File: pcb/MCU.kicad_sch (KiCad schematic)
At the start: 10 parts, among them U1 WeMos_S2_mini

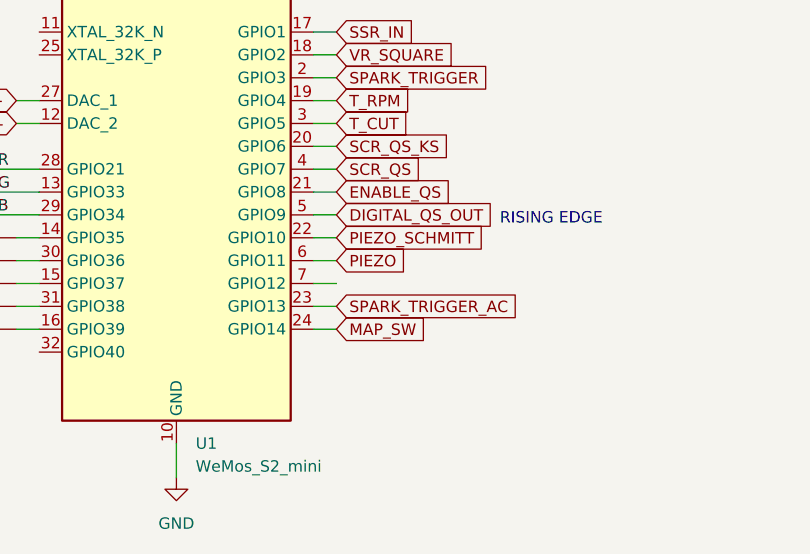
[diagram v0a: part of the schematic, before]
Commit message: widely changed TCI schematic to use a FET IC driver
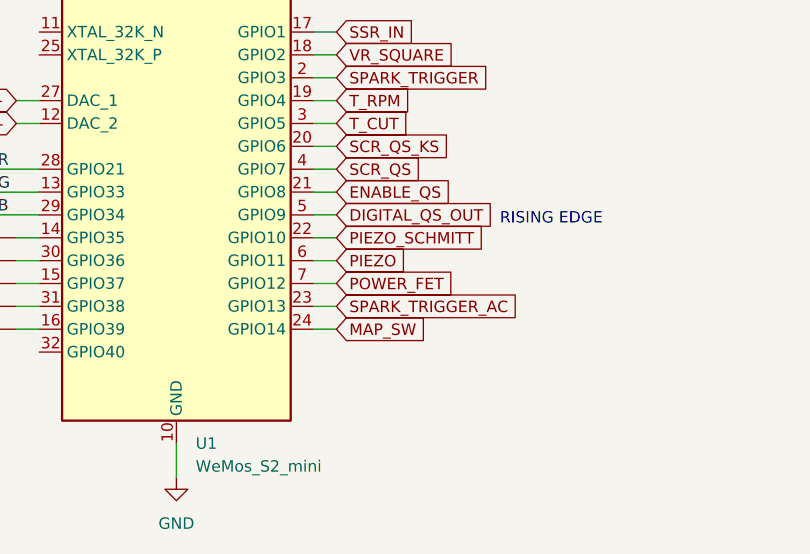
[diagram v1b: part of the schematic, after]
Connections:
- net POWER_FET: now reaches U1.7 (GPIO12)
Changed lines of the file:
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@@
+		)
+	)
+	(global_label "POWER_FET"
+		(shape input)
+		(at 106.68 80.01 0)
+		(fields_autoplaced yes)
+		(effects
+			(font
+				(size 1.27 1.27)
+			)
+			(justify left)
+		)
+		(property "Intersheetrefs" "${INTERSHEET_REFS}"
+			(at 120.3089 80.01 0)
+			(effects
+				(font
+					(size 1.27 1.27)
+				)
+				(justify left)
+				(hide yes)
+			)
 		)
 	)

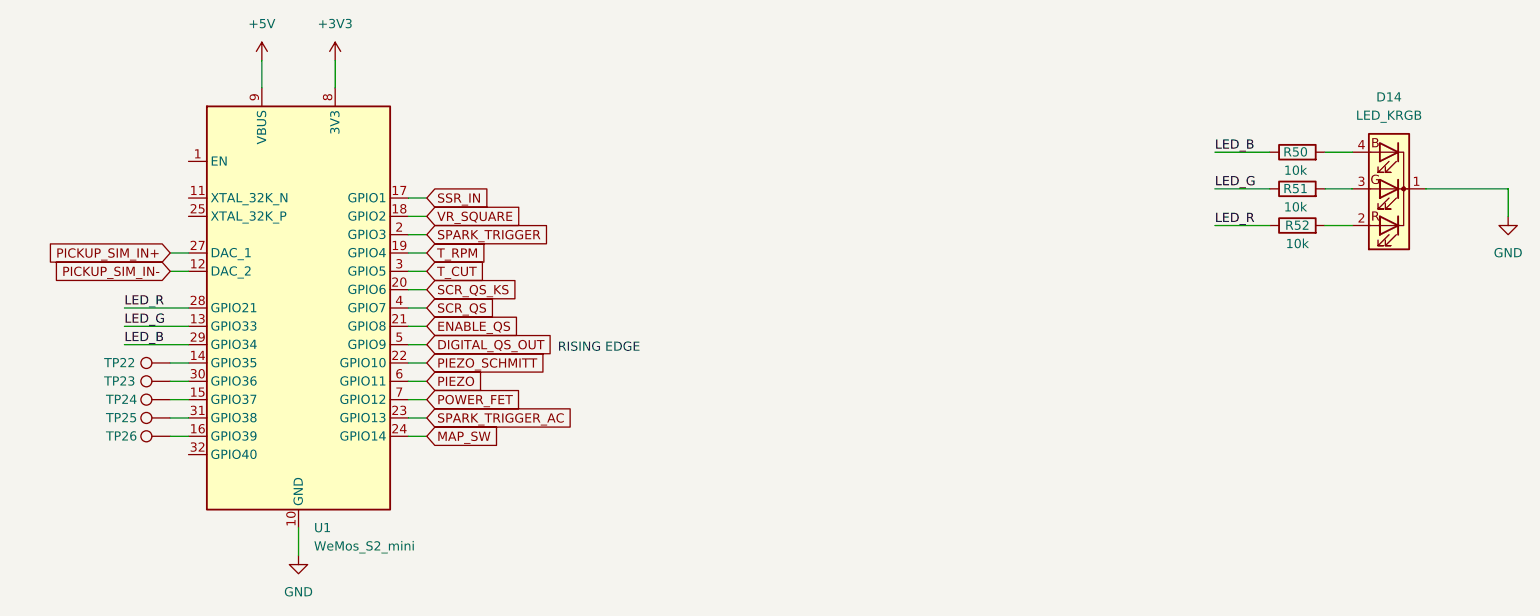
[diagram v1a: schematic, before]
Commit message: added DNP for fabrication and 2P molex connector, minor fixes
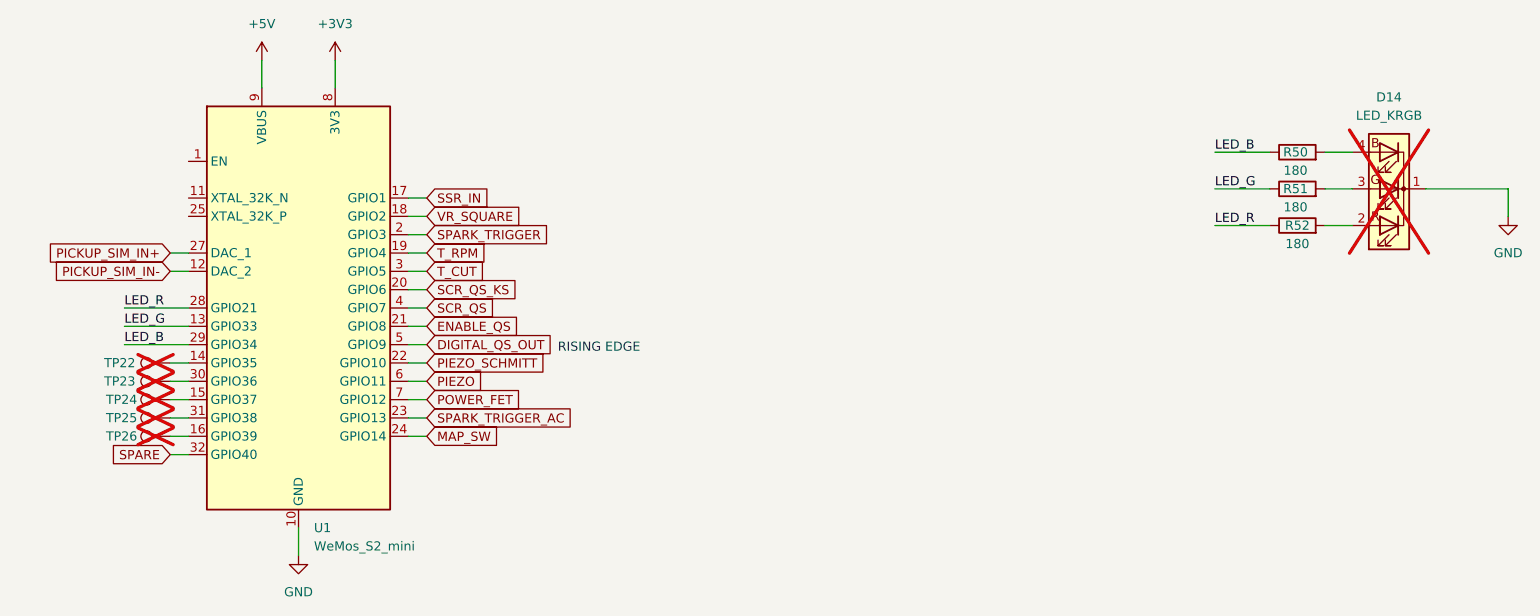
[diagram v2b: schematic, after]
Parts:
- D14: now not fitted
- R50, R51, R52: value 10k -> 180
- TP22, TP23, TP24, TP25, TP26: footprint Connector_PinHeader_1.00mm:PinHeader_1x01_P1.00mm_Vertical -> Connector_PinHeader_2.54mm:PinHeader_1x01_P2.54mm_Vertical; now not fitted
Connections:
- net SPARE: now reaches U1.32 (GPIO40)
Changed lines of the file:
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@@
+	(wire
+		(pts
+			(xy 71.12 87.63) (xy 73.66 87.63)
+		)
+		(stroke
+			(width 0)
+			(type default)
+		)
+	)
 	(wire
 		(pts
@@
 				)
 				(justify left)
+				(hide yes)
+			)
+		)
+	)
+	(global_label "SPARE"
+		(shape input)
+		(at 71.12 87.63 180)
+		(fields_autoplaced yes)
+		(effects
+			(font
+				(size 1.27 1.27)
+			)
+			(justify right)
+		)
+		(property "Intersheetrefs" "${INTERSHEET_REFS}"
+			(at 62.1477 87.63 0)
+			(effects
+				(font
+					(size 1.27 1.27)
+				)
+				(justify right)
 				(hide yes)
 			)
@@
 		(in_bom yes)
 		(on_board yes)
-		(dnp no)
+		(dnp yes)
 		(fields_autoplaced yes)
 		(property "Reference" "D14"
@@
 			)
 		)
-		(property "Value" "10k"
+		(property "Value" "180"
 			(at 227.076 48.26 90)
 			(effects
@@
 		(in_bom yes)
 		(on_board yes)
-		(dnp no)
+		(dnp yes)
 		(property "Reference" "TP23"
 			(at 66.294 77.47 90)
@@
 			)
 		)
-		(property "Footprint" "Connector_PinHeader_1.00mm:PinHeader_1x01_P1.00mm_Vertical"
+		(property "Footprint" "Connector_PinHeader_2.54mm:PinHeader_1x01_P2.54mm_Vertical"
 			(at 71.12 72.39 0)
 			(effects
@@
 			)
 		)
-		(property "Value" "10k"
+		(property "Value" "180"
 			(at 227.076 53.34 90)
 			(effects
@@
 		(in_bom yes)
 		(on_board yes)
-		(dnp no)
+		(dnp yes)
 		(property "Reference" "TP22"
 			(at 66.294 74.93 90)
@@
 			)
 		)
-		(property "Footprint" "Connector_PinHeader_1.00mm:PinHeader_1x01_P1.00mm_Vertical"
+		(property "Footprint" "Connector_PinHeader_2.54mm:PinHeader_1x01_P2.54mm_Vertical"
 			(at 71.12 69.85 0)
 			(effects
@@
 		(in_bom yes)
 		(on_board yes)
-		(dnp no)
+		(dnp yes)
 		(property "Reference" "TP24"
 			(at 66.548 80.01 90)
@@
 			)
 		)
-		(property "Footprint" "Connector_PinHeader_1.00mm:PinHeader_1x01_P1.00mm_Vertical"
+		(property "Footprint" "Connector_PinHeader_2.54mm:PinHeader_1x01_P2.54mm_Vertical"
 			(at 71.12 74.93 0)
 			(effects
@@
 		(in_bom yes)
 		(on_board yes)
-		(dnp no)
+		(dnp yes)
 		(property "Reference" "TP25"
 			(at 66.548 82.55 90)
@@
 			)
 		)
-		(property "Footprint" "Connector_PinHeader_1.00mm:PinHeader_1x01_P1.00mm_Vertical"
+		(property "Footprint" "Connector_PinHeader_2.54mm:PinHeader_1x01_P2.54mm_Vertical"
 			(at 71.12 77.47 0)
 			(effects
@@
 			)
 		)
-		(property "Value" "10k"
+		(property "Value" "180"
 			(at 227.33 58.42 90)
 			(effects
@@
 		(in_bom yes)
 		(on_board yes)
-		(dnp no)
+		(dnp yes)
 		(property "Reference" "TP26"
 			(at 66.548 85.09 90)
@@
 			)
 		)
-		(property "Footprint" "Connector_PinHeader_1.00mm:PinHeader_1x01_P1.00mm_Vertical"
+		(property "Footprint" "Connector_PinHeader_2.54mm:PinHeader_1x01_P2.54mm_Vertical"
 			(at 71.12 80.01 0)
 			(effects

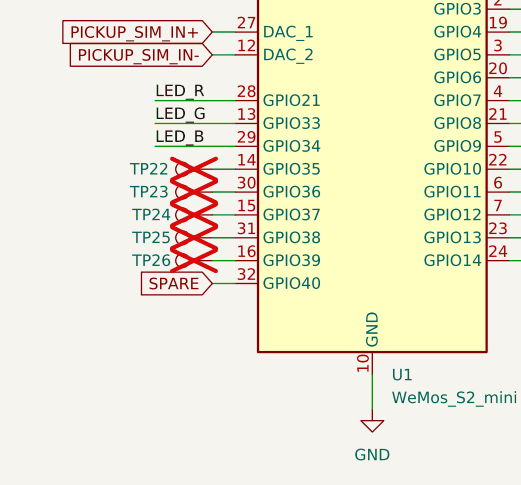
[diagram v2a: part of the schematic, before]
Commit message: added another CDI output sensing (opto coupler)
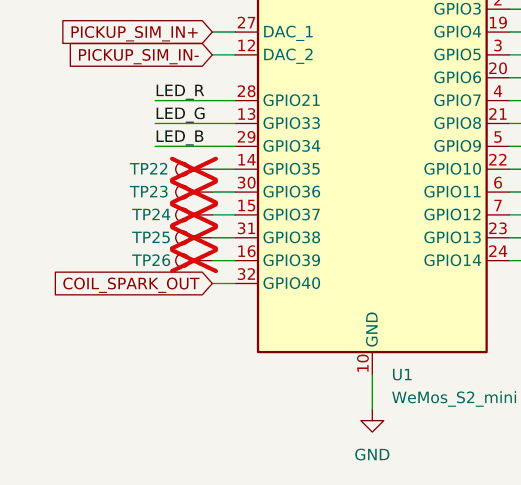
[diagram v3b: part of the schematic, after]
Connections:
- net SPARE renamed COIL_SPARK_OUT
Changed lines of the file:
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@@
+		)
+	)
+	(global_label "COIL_SPARK_OUT"
+		(shape input)
+		(at 71.12 87.63 180)
+		(fields_autoplaced yes)
+		(effects
+			(font
+				(size 1.27 1.27)
+			)
+			(justify right)
+		)
+		(property "Intersheetrefs" "${INTERSHEET_REFS}"
+			(at 52.2295 87.63 0)
+			(effects
+				(font
+					(size 1.27 1.27)
+				)
+				(justify right)
+				(hide yes)
+			)
 		)
 	)
@@
 				(hide yes)
 			)
-		)
-	)
-	(global_label "SPARE"
-		(shape input)
-		(at 71.12 87.63 180)
-		(fields_autoplaced yes)
-		(effects
-			(font
-				(size 1.27 1.27)
-			)
-			(justify right)
-		)
-		(property "Intersheetrefs" "${INTERSHEET_REFS}"
-			(at 62.1477 87.63 0)
-			(effects
-				(font
-					(size 1.27 1.27)
-				)
-				(justify right)
-				(hide yes)
-			)

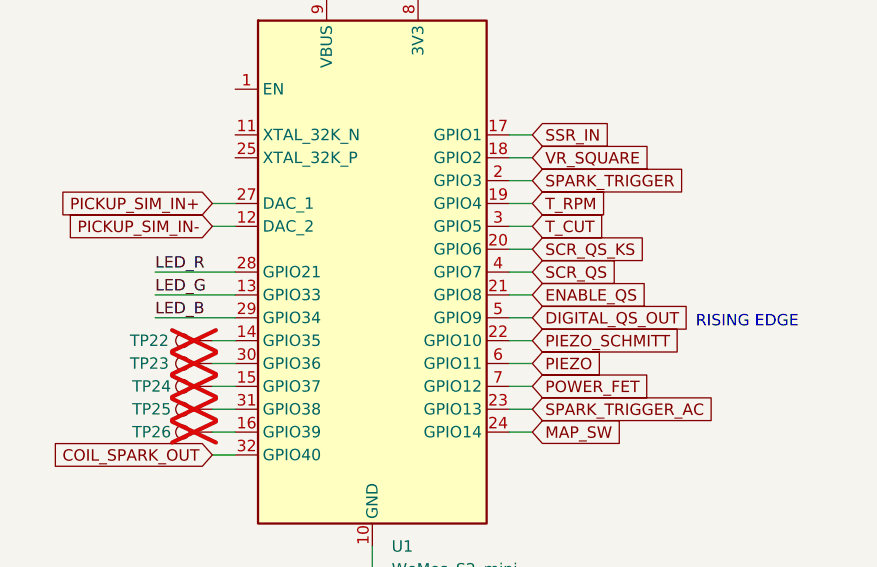
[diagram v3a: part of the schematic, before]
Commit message: added pull-downs to QS stuff
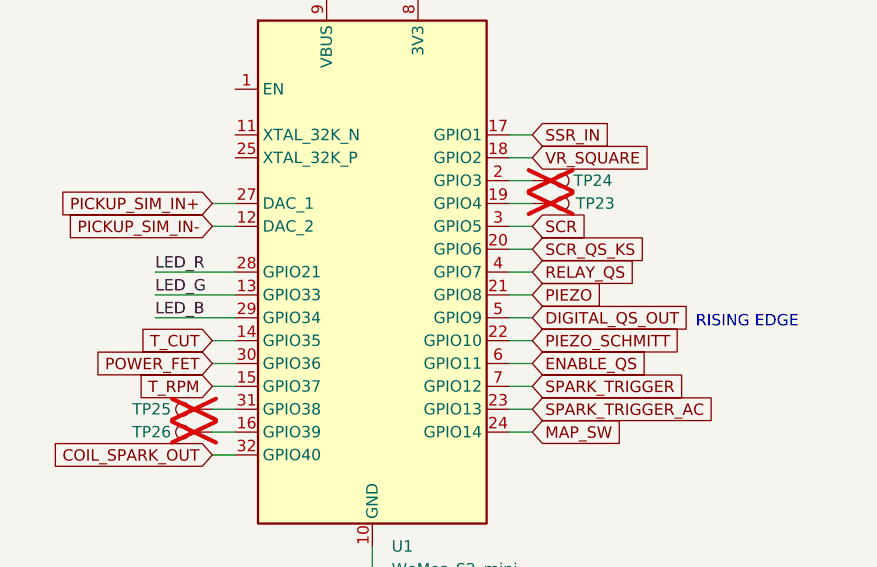
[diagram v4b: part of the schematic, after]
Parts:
- removed TP22: TestPoint, Connector_PinHeader_2.54mm:PinHeader_1x01_P2.54mm_Vertical, symbol Connector:TestPoint
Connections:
- net ENABLE_QS: now also U1.6 (GPIO11); no longer U1.21 (GPIO8)
- net PIEZO: now also U1.21 (GPIO8); no longer U1.6 (GPIO11)
- net POWER_FET: now also U1.30 (GPIO36); no longer U1.7 (GPIO12)
- net SPARK_TRIGGER: now also U1.7 (GPIO12); no longer U1.2 (GPIO3)
- net T_CUT: now also U1.14 (GPIO35); no longer U1.3 (GPIO5)
- net T_RPM: now also U1.15 (GPIO37); no longer U1.19 (GPIO4)
- net at TP23.1: now also U1.19 (GPIO4); no longer U1.30 (GPIO36)
- net at TP24.1: now also U1.2 (GPIO3); no longer U1.15 (GPIO37)
- net SCR_QS renamed RELAY_QS
- new net SCR: U1.3 (GPIO5)
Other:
- moved on the sheet: TP23, TP24

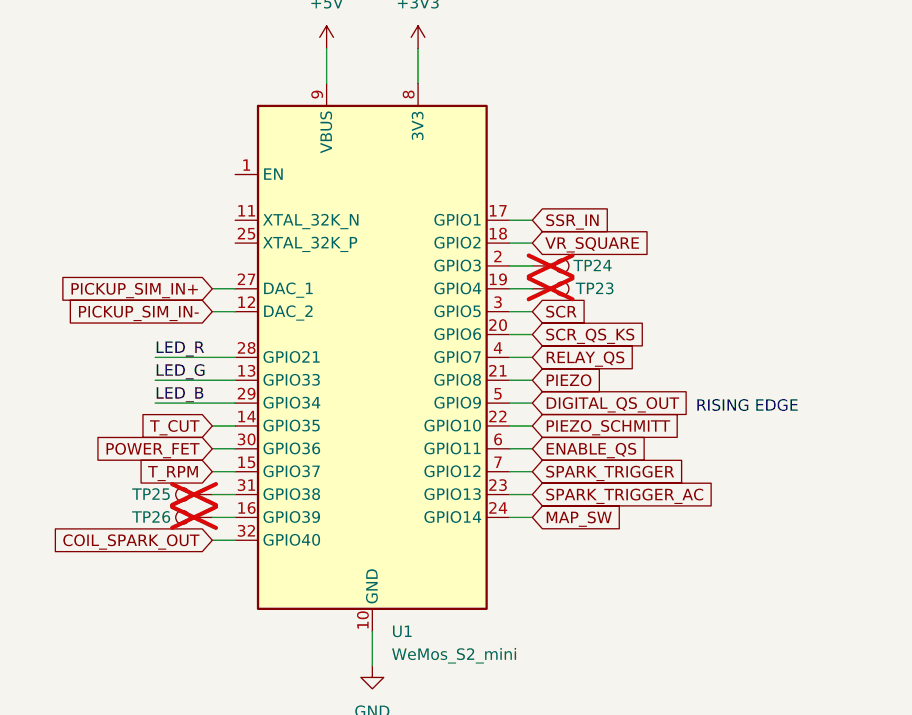
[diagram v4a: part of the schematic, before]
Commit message: MCU labels rework
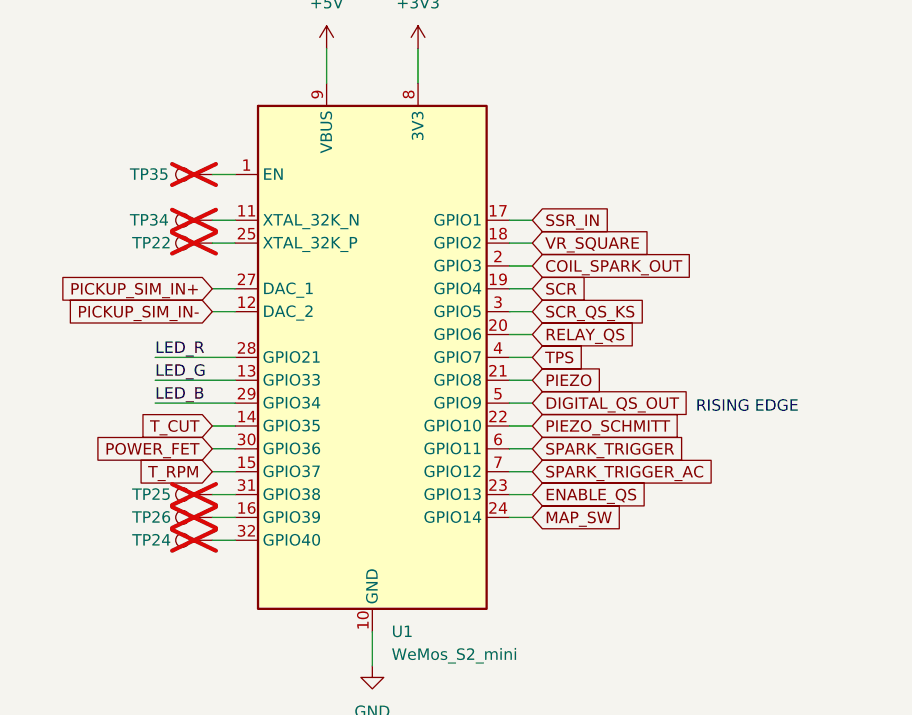
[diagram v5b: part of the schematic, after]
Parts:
- removed TP23: TestPoint, Connector_PinHeader_2.54mm:PinHeader_1x01_P2.54mm_Vertical, symbol Connector:TestPoint
- added TP22, TP34, TP35: TestPoint, Connector_PinHeader_2.54mm:PinHeader_1x01_P2.54mm_Vertical, symbol Connector:TestPoint
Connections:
- net COIL_SPARK_OUT: now also U1.2 (GPIO3); no longer U1.32 (GPIO40)
- net ENABLE_QS: now also U1.23 (GPIO13); no longer U1.6 (GPIO11)
- net RELAY_QS: now also U1.20 (GPIO6); no longer U1.4 (GPIO7)
- net SCR: now also U1.19 (GPIO4); no longer U1.3 (GPIO5)
- net SCR_QS_KS: now also U1.3 (GPIO5); no longer U1.20 (GPIO6)
- net SPARK_TRIGGER: now also U1.6 (GPIO11); no longer U1.7 (GPIO12)
- net SPARK_TRIGGER_AC: now also U1.7 (GPIO12); no longer U1.23 (GPIO13)
- net at U1.1 (EN): now also TP35.1
- net at U1.11 (XTAL_32K_N): now also TP34.1
- net at TP24.1: now also U1.32 (GPIO40); no longer U1.2 (GPIO3)
- net at U1.25 (XTAL_32K_P): now also TP22.1
- new net TPS: U1.4 (GPIO7)
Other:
- moved on the sheet: TP24

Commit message: revision 2.0: changed components numeration
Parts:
- renumbered D14 to D301, R50 to R301, R51 to R302, R52 to R303, TP35 to TP301, TP34 to TP302, TP22 to TP303, TP25 to TP304, TP26 to TP305, TP24 to TP306, U1 to U301
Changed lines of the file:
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@@
 		(dnp no)
 		(fields_autoplaced yes)
-		(property "Reference" "#PWR08"
+		(property "Reference" "#PWR0301"
 			(at 83.82 36.83 0)
 			(effects
@@
 			(project ""
 				(path "/38d4df77-b5a0-4642-8410-8b13c21c2c3b/5baacb37-d82a-49c1-a6be-f8a839583d33"
-					(reference "#PWR08")
+					(reference "#PWR0301")
 					(unit 1)
 				)
@@
 		(dnp yes)
 		(fields_autoplaced yes)
-		(property "Reference" "D14"
+		(property "Reference" "D301"
 			(at 240.03 38.1 0)
 			(effects
@@
 			(project ""
 				(path "/38d4df77-b5a0-4642-8410-8b13c21c2c3b/5baacb37-d82a-49c1-a6be-f8a839583d33"
-					(reference "D14")
+					(reference "D301")
 					(unit 1)
 				)
@@
 		(on_board yes)
 		(dnp yes)
-		(property "Reference" "TP22"
+		(property "Reference" "TP303"
 			(at 66.548 54.61 90)
 			(effects
@@
 			(project "ecu-dev-board"
 				(path "/38d4df77-b5a0-4642-8410-8b13c21c2c3b/5baacb37-d82a-49c1-a6be-f8a839583d33"
-					(reference "TP22")
+					(reference "TP303")
 					(unit 1)
 				)
@@
 		(on_board yes)
 		(dnp no)
-		(property "Reference" "R50"
+		(property "Reference" "R301"
 			(at 227.076 45.72 90)
 			(effects
@@
 			(project "ecu-dev-board"
 				(path "/38d4df77-b5a0-4642-8410-8b13c21c2c3b/5baacb37-d82a-49c1-a6be-f8a839583d33"
-					(reference "R50")
+					(reference "R301")
 					(unit 1)
 				)
@@
 		(dnp no)
 		(fields_autoplaced yes)
-		(property "Reference" "#PWR07"
+		(property "Reference" "#PWR0303"
 			(at 93.98 36.83 0)
 			(effects
@@
 			(project ""
 				(path "/38d4df77-b5a0-4642-8410-8b13c21c2c3b/5baacb37-d82a-49c1-a6be-f8a839583d33"
-					(reference "#PWR07")
+					(reference "#PWR0303")
 					(unit 1)
 				)
@@
 		(on_board yes)
 		(dnp yes)
-		(property "Reference" "TP34"
+		(property "Reference" "TP302"
 			(at 66.294 52.07 90)
 			(effects
@@
 			(project "ecu-dev-board"
 				(path "/38d4df77-b5a0-4642-8410-8b13c21c2c3b/5baacb37-d82a-49c1-a6be-f8a839583d33"
-					(reference "TP34")
+					(reference "TP302")
 					(unit 1)
 				)
@@
 		(on_board yes)
 		(dnp yes)
-		(property "Reference" "TP35"
+		(property "Reference" "TP301"
 			(at 66.294 46.99 90)
 			(effects
@@
 			(project "ecu-dev-board"
 				(path "/38d4df77-b5a0-4642-8410-8b13c21c2c3b/5baacb37-d82a-49c1-a6be-f8a839583d33"
-					(reference "TP35")
+					(reference "TP301")
 					(unit 1)
 				)
@@
 		(dnp no)
 		(fields_autoplaced yes)
-		(property "Reference" "#PWR053"
+		(property "Reference" "#PWR0304"
 			(at 256.54 60.96 0)
 			(effects
@@
 			(project ""
 				(path "/38d4df77-b5a0-4642-8410-8b13c21c2c3b/5baacb37-d82a-49c1-a6be-f8a839583d33"
-					(reference "#PWR053")
+					(reference "#PWR0304")
 					(unit 1)
 				)
@@
 		(on_board yes)
 		(dnp no)
-		(property "Reference" "R51"
+		(property "Reference" "R302"
 			(at 227.076 50.8 90)
 			(effects
@@
 			(project "ecu-dev-board"
 				(path "/38d4df77-b5a0-4642-8410-8b13c21c2c3b/5baacb37-d82a-49c1-a6be-f8a839583d33"
-					(reference "R51")
+					(reference "R302")
 					(unit 1)
 				)
@@
 		(dnp no)
 		(fields_autoplaced yes)
-		(property "Reference" "U1"
+		(property "Reference" "U301"
 			(at 91.0433 97.79 0)
 			(effects
@@
 			(project ""
 				(path "/38d4df77-b5a0-4642-8410-8b13c21c2c3b/5baacb37-d82a-49c1-a6be-f8a839583d33"
-					(reference "U1")
+					(reference "U301")
 					(unit 1)
 				)
@@
 		(on_board yes)
 		(dnp yes)
-		(property "Reference" "TP24"
+		(property "Reference" "TP306"
 			(at 66.548 87.63 90)
 			(effects
@@
 			(project "ecu-dev-board"
 				(path "/38d4df77-b5a0-4642-8410-8b13c21c2c3b/5baacb37-d82a-49c1-a6be-f8a839583d33"
-					(reference "TP24")
+					(reference "TP306")
 					(unit 1)
 				)
@@
 		(on_board yes)
 		(dnp yes)
-		(property "Reference" "TP25"
+		(property "Reference" "TP304"
 			(at 66.548 82.55 90)
 			(effects
@@
 			(project "ecu-dev-board"
 				(path "/38d4df77-b5a0-4642-8410-8b13c21c2c3b/5baacb37-d82a-49c1-a6be-f8a839583d33"
-					(reference "TP25")
+					(reference "TP304")
 					(unit 1)
 				)
@@
 		(dnp no)
 		(fields_autoplaced yes)
-		(property "Reference" "#PWR06"
+		(property "Reference" "#PWR0302"
 			(at 88.9 107.95 0)
 			(effects
@@
 			(project ""
 				(path "/38d4df77-b5a0-4642-8410-8b13c21c2c3b/5baacb37-d82a-49c1-a6be-f8a839583d33"
-					(reference "#PWR06")
+					(reference "#PWR0302")
 					(unit 1)
 				)
@@
 		(on_board yes)
 		(dnp no)
-		(property "Reference" "R52"
+		(property "Reference" "R303"
 			(at 227.33 55.88 90)
 			(effects
@@
 			(project "ecu-dev-board"
 				(path "/38d4df77-b5a0-4642-8410-8b13c21c2c3b/5baacb37-d82a-49c1-a6be-f8a839583d33"
-					(reference "R52")
+					(reference "R303")
 					(unit 1)
 				)
@@
 		(on_board yes)
 		(dnp yes)
-		(property "Reference" "TP26"
+		(property "Reference" "TP305"
 			(at 66.548 85.09 90)
 			(effects
@@
 			(project "ecu-dev-board"
 				(path "/38d4df77-b5a0-4642-8410-8b13c21c2c3b/5baacb37-d82a-49c1-a6be-f8a839583d33"
-					(reference "TP26")
-					(unit 1)
-				)
+					(reference "TP305")
+					(unit 1)
+				)
